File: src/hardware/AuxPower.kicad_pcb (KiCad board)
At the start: 2 copper layers, 90 x 90 mm, 104 parts, among them J1 MC 1,5/2, J10 MC 1,5/4, J11 S3B-XH-A, J12 S3B-XH-A, J13 S3B-XH-A, J14 S3B-XH-A, J15 S3B-XH-A, J16 B3B-XH-A, J17 B4B-XH-A, J2 MC 1,5/2, J3 MC 1,5/2, J4 MC 1,5/2, J5 MC 1,5/2, J6 MC 1,5/4, J7 MC 1,5/4, J8 MC 1,5/4, J9 MC 1,5/4, U1 ZXCT1009, U2 ZXCT1009, U3 ZXCT1009, U4 ZXCT1009, U5 ZXCT1009, U6 PIC18F26K83, U7 PI4IOE5V6416, U8 MCP9701

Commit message: Fixed current monitor part name
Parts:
- U1, U2, U3, U4, U5: value ZXCT1009 -> HV7801
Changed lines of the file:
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@@
 			)
 		)
-		(property "Value" "ZXCT1009"
+		(property "Value" "HV7801"
 			(at 0 -2.4 90)
 			(layer "B.SilkS")
@@
 			)
 		)
-		(property "Value" "ZXCT1009"
+		(property "Value" "HV7801"
 			(at 0 -2.4 90)
 			(layer "B.SilkS")
@@
 			)
 		)
-		(property "Value" "ZXCT1009"
+		(property "Value" "HV7801"
 			(at 0 -2.4 90)
 			(layer "B.SilkS")
@@
 			)
 		)
-		(property "Value" "ZXCT1009"
+		(property "Value" "HV7801"
 			(at 0 -2.4 90)
 			(layer "B.SilkS")
@@
 			)
 		)
-		(property "Value" "ZXCT1009"
+		(property "Value" "HV7801"
 			(at 0 -2.4 90)
 			(layer "B.SilkS")

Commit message: Adjusted current monitor resistor for 1:1 ratio
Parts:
- R11, R12, R13, R14, R15: value 1K -> 1K07
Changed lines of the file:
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@@
 			)
 		)
-		(property "Value" "1K"
+		(property "Value" "1K07"
 			(at -2.35 0 0)
 			(layer "B.SilkS")
@@
 			)
 		)
-		(property "Value" "1K"
+		(property "Value" "1K07"
 			(at -2.35 0 0)
 			(layer "B.SilkS")
@@
 			)
 		)
-		(property "Value" "1K"
+		(property "Value" "1K07"
 			(at -2.375 0 0)
 			(layer "B.SilkS")
@@
 			)
 		)
-		(property "Value" "1K"
+		(property "Value" "1K07"
 			(at -2.4 0 0)
 			(layer "B.SilkS")
@@
 			)
 		)
-		(property "Value" "1K"
+		(property "Value" "1K07"
 			(at -2.35 0 0)
 			(layer "B.SilkS")

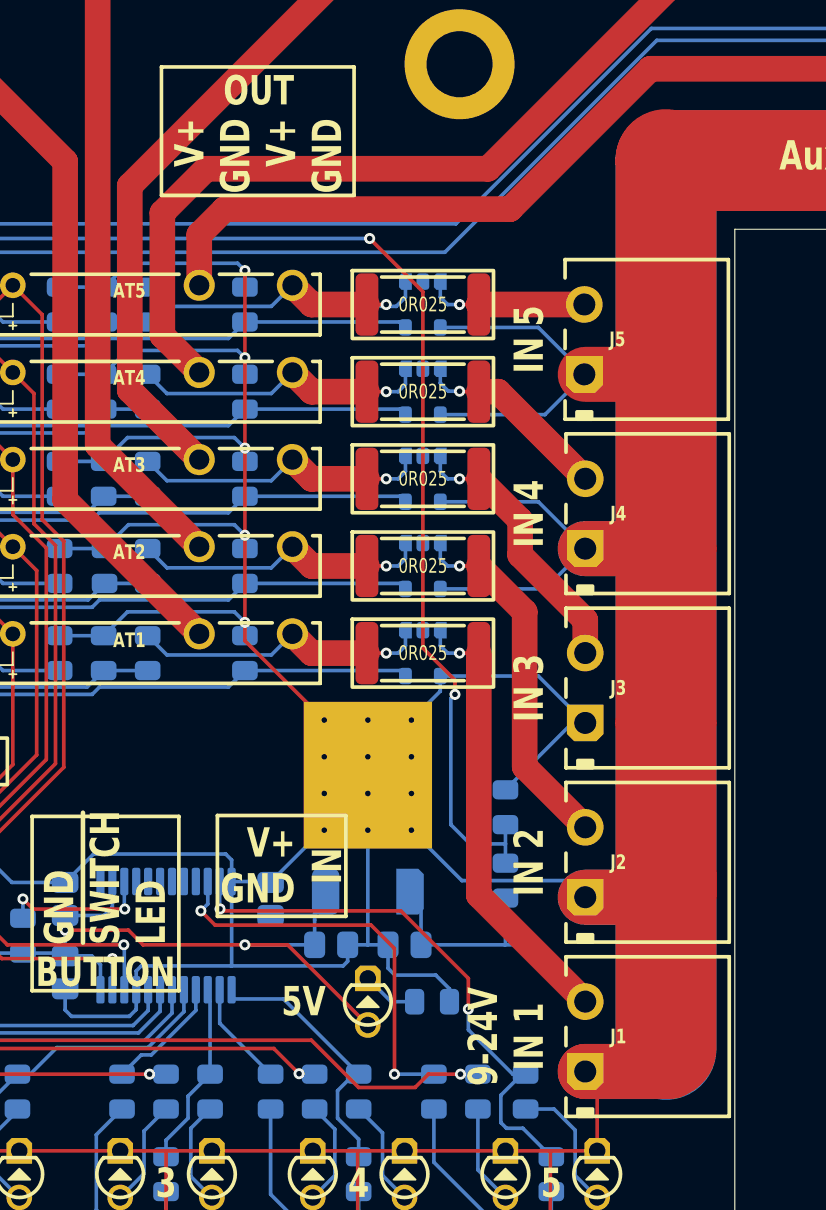
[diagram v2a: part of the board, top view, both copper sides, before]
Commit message: Updated photomos refdes
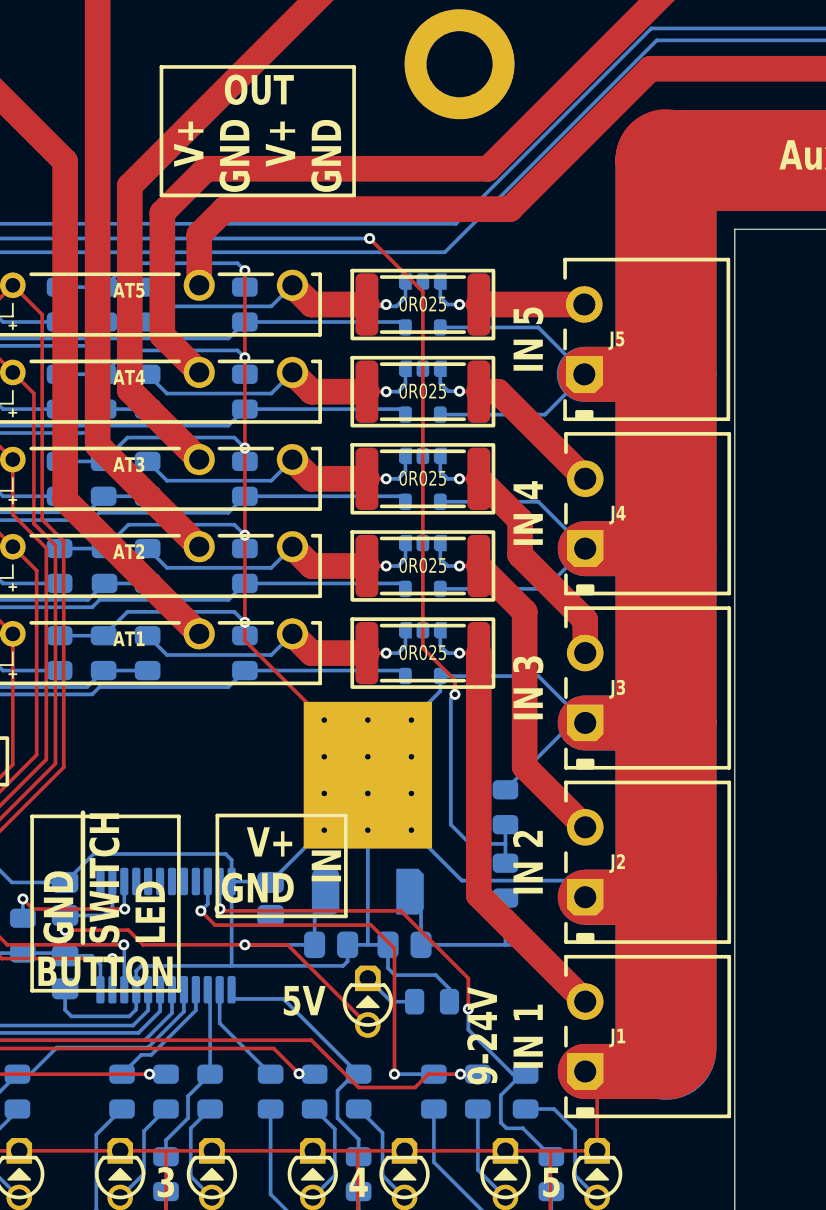
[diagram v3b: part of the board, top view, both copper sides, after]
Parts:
- AT3: footprint Medo64:AY PhotoMOS [AQZ202G] (SIP-4) -> Medo64:AT PhotoMOS [AQZ202G] (SIP-4)
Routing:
- net GND: track 846.8 -> 860.1 mm
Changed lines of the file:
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@@
 		(descr "Panasonic AQZ202G")
 		(property "Reference" "AT1"
-			(at 0 0.35 0)
+			(at 0 0.3 0)
 			(layer "F.SilkS")
 			(effects
@@
 		)
 		(property "Value" "AQZ202G"
-			(at 0 1.75 0)
+			(at 0 1.7 0)
 			(layer "F.Fab")
 			(effects
@@
 		)
 	)
-	(footprint "Medo64:AY PhotoMOS [AQZ202G] (SIP-4)"
+	(footprint "Medo64:AT PhotoMOS [AQZ202G] (SIP-4)"
 		(layer "F.Cu")
 		(at 42 52.55)
@@
 	)
 	(segment
+		(start 66.85 66.905)
+		(end 71.249998 66.905)
+		(width 3)
+		(layer "F.Cu")
+		(net 1)
+	)
+	(segment
 		(start 67.5 90.23)
 		(end 67.5 86.555)
@@
 	)
 	(segment
+		(start 71.249998 66.905)
+		(end 71.25 66.905002)
+		(width 0.2)
+		(layer "F.Cu")
+		(net 1)
+	)
+	(segment
 		(start 75.095 19.105)
 		(end 75.15 19.05)
@@
 	)
 	(segment
+		(start 71.25 84.7)
+		(end 71.25 66.9)
+		(width 5.5)
+		(layer "B.Cu")
+		(net 1)
+	)
+	(segment
 		(start 99.715 23)
 		(end 99.715 19.265002)
@@
 	)
 	(segment
-		(start 71.25 84.7)
+		(start 71.25 47.9)
 		(end 71.25 36.25)
 		(width 5.5)
@@
 	)
 	(segment
+		(start 71.245 47.905)
+		(end 71.25 47.9)
+		(width 0.2)
+		(layer "B.Cu")
+		(net 1)
+	)
+	(segment
 		(start 56.1 79)
 		(end 55 79)
@@
 	)
 	(segment
+		(start 66.85 66.905)
+		(end 71.245 66.905)
+		(width 3)
+		(layer "B.Cu")
+		(net 1)
+	)
+	(segment
 		(start 64.295 64.35)
 		(end 66.85 66.905)
@@
 	)
 	(segment
+		(start 71.245 66.905)
+		(end 71.25 66.9)
+		(width 0.2)
+		(layer "B.Cu")
+		(net 1)
+	)
+	(segment
 		(start 56.475 80.65)
 		(end 58.7 80.65)
@@
 	)
 	(segment
+		(start 66.8 47.905)
+		(end 71.245 47.905)
+		(width 3)
+		(layer "B.Cu")
+		(net 1)
+	)
+	(segment
 		(start 42.65 80.15)
 		(end 42.375 80.425)
@@
 		(layer "B.Cu")
 		(net 1)
+	)
+	(segment
+		(start 71.25 66.9)
+		(end 71.25 47.9)
+		(width 5.5)
+		(layer "B.Cu")
+		(net 1)

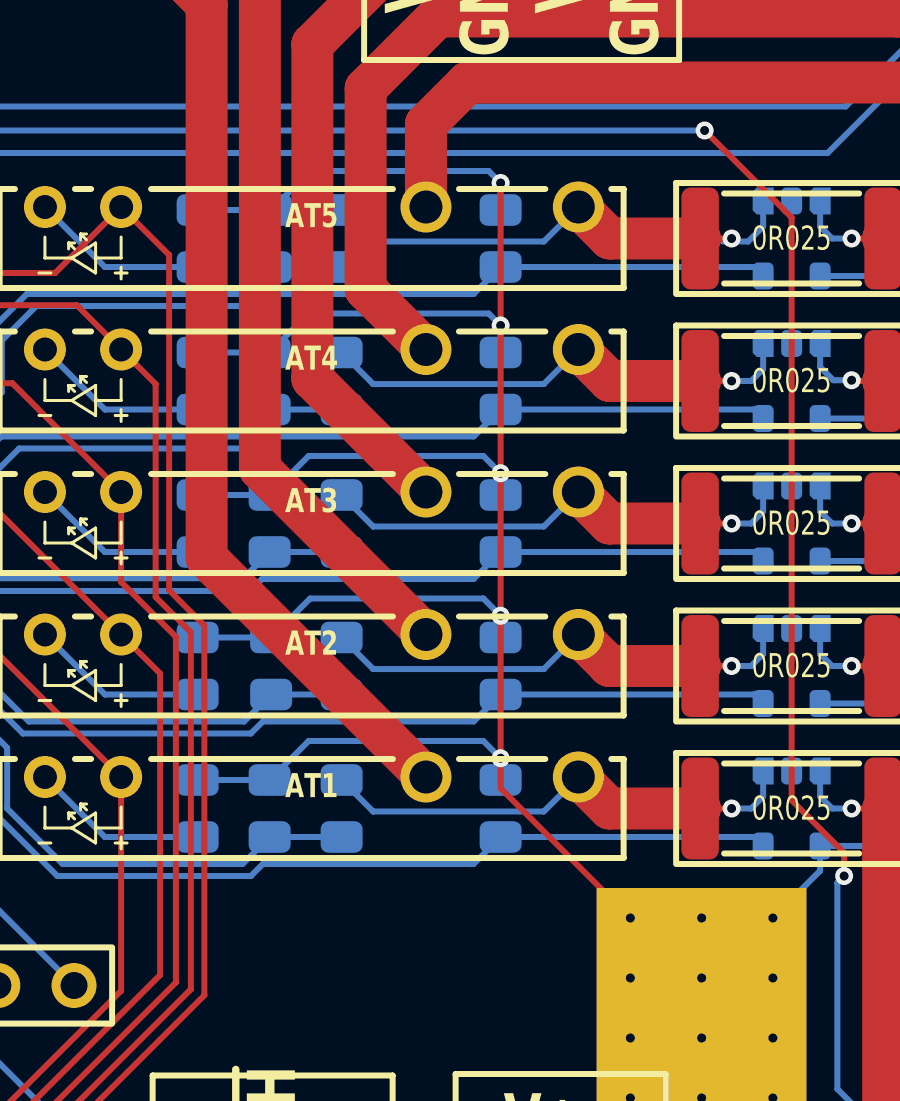
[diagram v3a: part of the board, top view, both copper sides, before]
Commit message: Removed HV7801 resistor
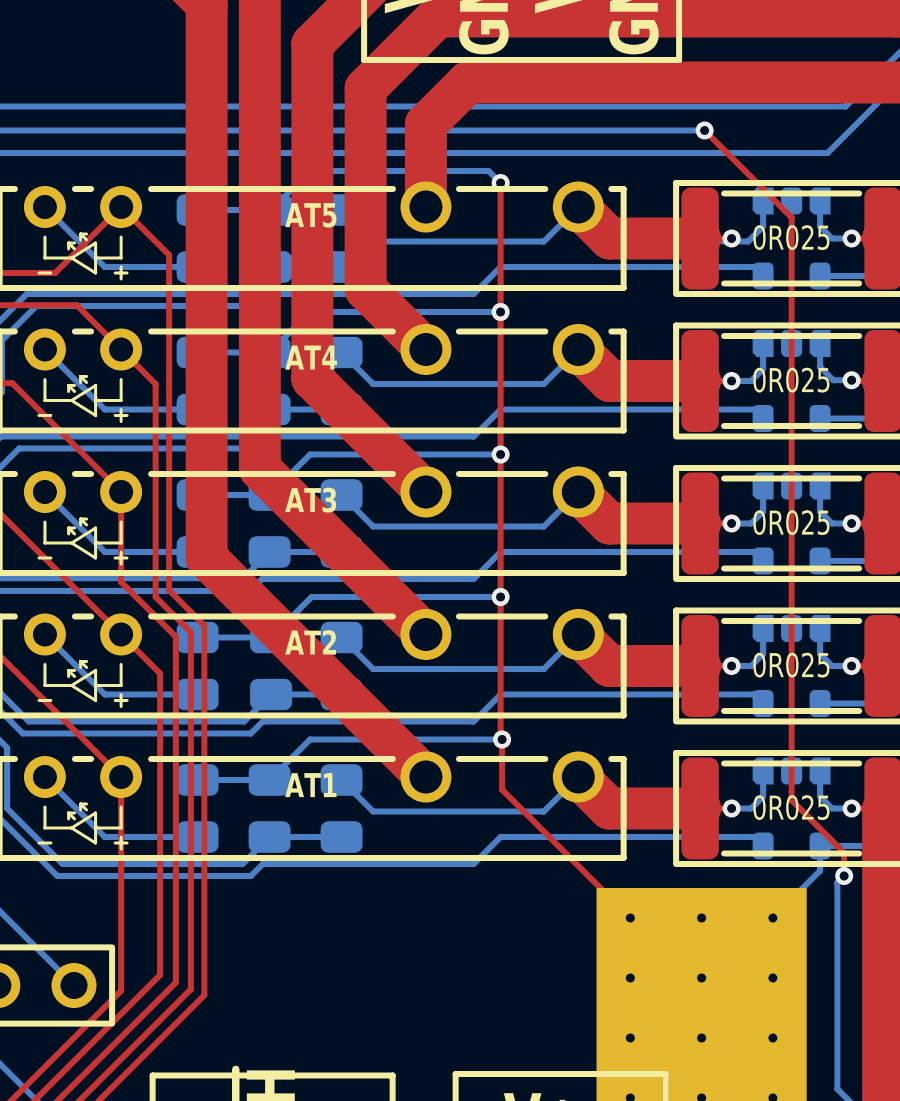
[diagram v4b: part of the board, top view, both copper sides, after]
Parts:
- removed the R11 at (48.3, 63.1)
- removed the R12 at (48.3, 58.4)
- removed the R13 at (48.3, 53.6)
- removed the R14 at (48.3, 48.9)
- removed the R15 at (48.3, 44.1)
- renumbered R16 to R11, R17 to R12, R18 to R13, R19 to R14, R20 to R15, R21 to R16, R22 to R17, R23 to R18, R24 to R19, R25 to R20, R26 to R21, R27 to R22, R28 to R23, R29 to R24, R30 to R25, R31 to R26, R32 to R27, R33 to R28, R34 to R29, R35 to R30, R36 to R31, R37 to R32, R38 to R33, R39 to R34, R40 to R35, R41 to R36, R42 to R37, R43 to R38, R44 to R39, R45 to R40, R46 to R41, R47 to R42, R48 to R43, R49 to R44, R50 to R45, R51 to R46, R52 to R47
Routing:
- net GND: track 860.1 -> 855.4 mm
